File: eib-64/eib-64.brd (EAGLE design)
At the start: 15.9 x 15.8 mm, 25 parts, among them J1 DF40-REC

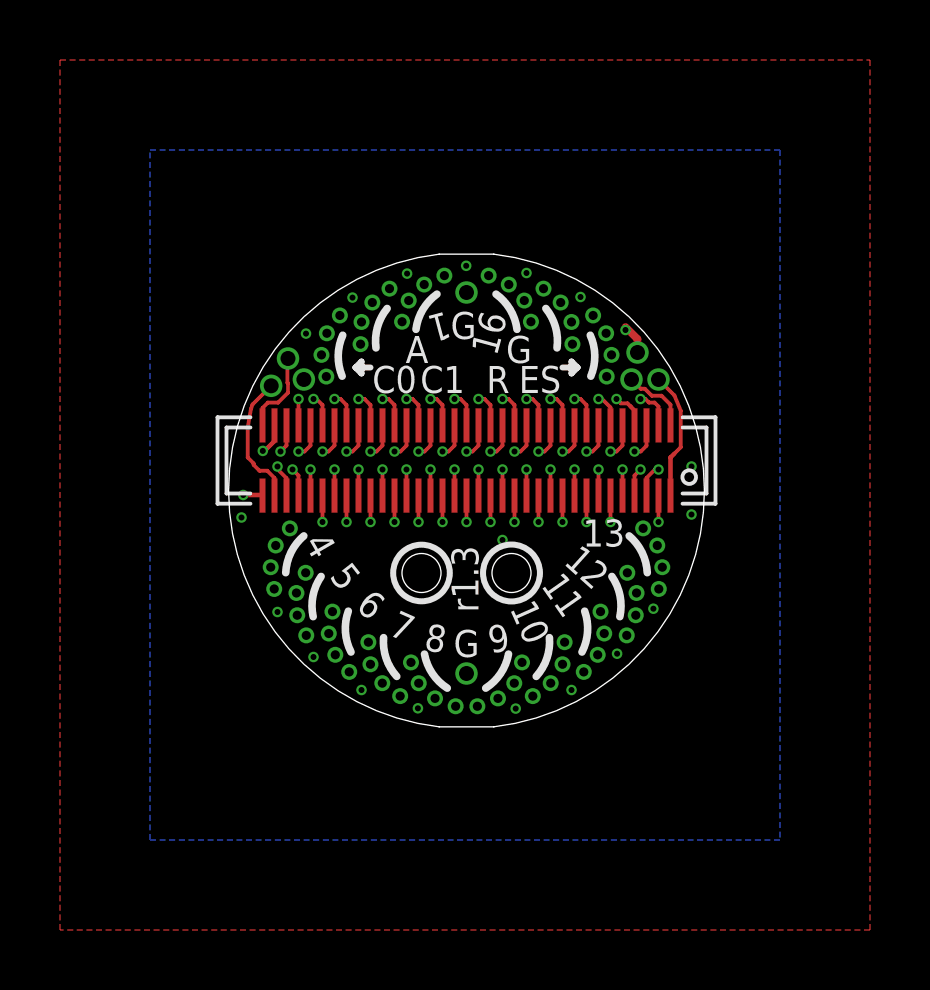
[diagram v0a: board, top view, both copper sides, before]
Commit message: Updated the layout with an extra hole for a fiber.
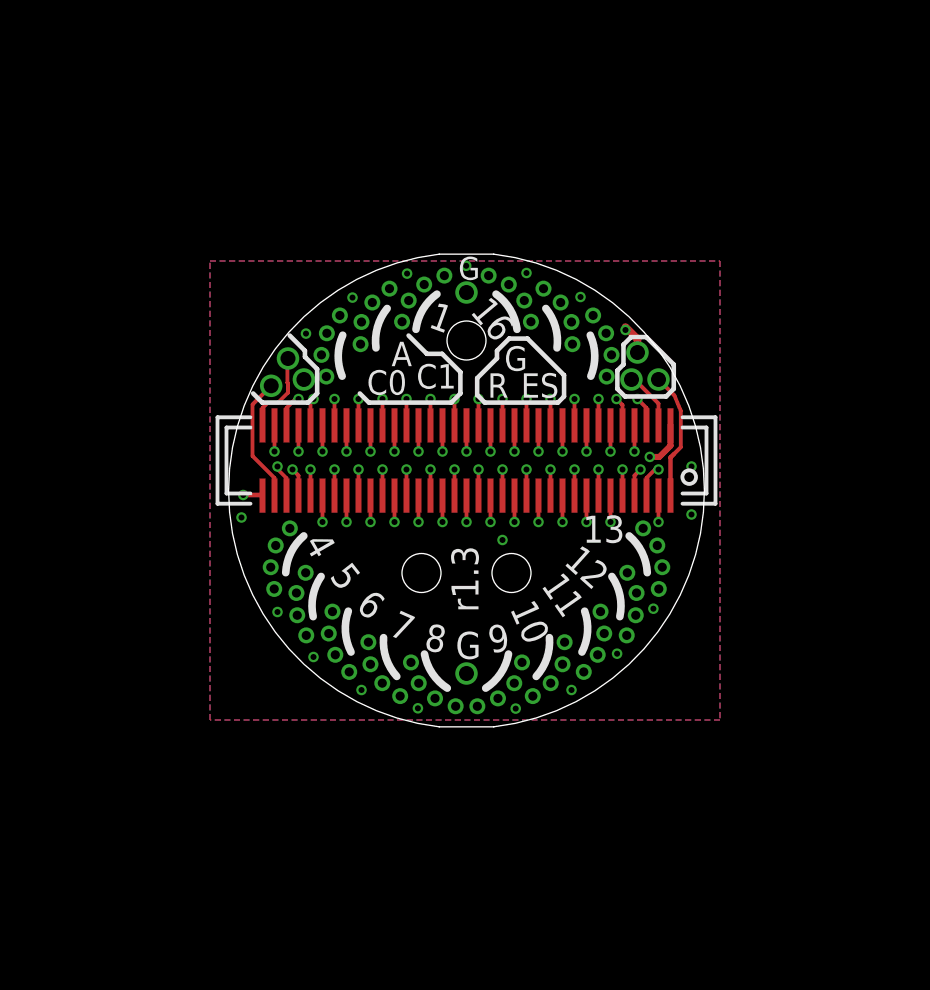
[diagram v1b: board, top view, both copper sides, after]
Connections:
- net GND: now also J1.70; no longer J1.37
- net N$1: now also J1.68; no longer J1.69
- net N$10: now also J1.59; no longer J1.60
- net N$11: now also J1.58; no longer J1.59
- net N$12: now also J1.57; no longer J1.58
- net N$13: now also J1.56; no longer J1.57
- net N$14: now also J1.55; no longer J1.56
- net N$15: now also J1.54; no longer J1.55
- net N$16: now also J1.53; no longer J1.54
- net N$17: now also J1.52; no longer J1.53
- net N$18: now also J1.51; no longer J1.52
- net N$19: now also J1.50; no longer J1.51
- net N$2: now also J1.65; no longer J1.66
- net N$20: now also J1.49; no longer J1.50
- net N$21: now also J1.48; no longer J1.49
- net N$22: now also J1.47; no longer J1.48
- net N$23: now also J1.46; no longer J1.47
- net N$24: now also J1.45; no longer J1.46
- net N$25: now also J1.44; no longer J1.45
- net N$26: now also J1.43; no longer J1.44
- net N$27: now also J1.42; no longer J1.43
- net N$28: now also J1.41; no longer J1.42
- net N$29: now also J1.40; no longer J1.41
- net N$3: now also J1.66; no longer J1.67
- net N$30: now also J1.39; no longer J1.40
- net N$31: now also J1.38; no longer J1.39
- net N$32: now also J1.37; no longer J1.38
- net N$4: now also J1.67; no longer J1.68
- net N$5: now also J1.64; no longer J1.65
- net N$6: now also J1.63; no longer J1.64
- net N$7: now also J1.62; no longer J1.63
- net N$8: now also J1.61; no longer J1.62
- net N$9: now also J1.60; no longer J1.61
- net REF: now also J1.69; no longer J1.70
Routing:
- net N$29: track 7.07 -> 6.40 mm
- net N$3: track 7.40 -> 6.77 mm
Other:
- board text added: "EIB-64, r1.3 Open Ephys"
- board text removed: "EIB-64, r1.2 JPN & Open Ephys OHL v1.2 '19"
